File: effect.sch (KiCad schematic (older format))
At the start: 29 parts, among them U5 TL072

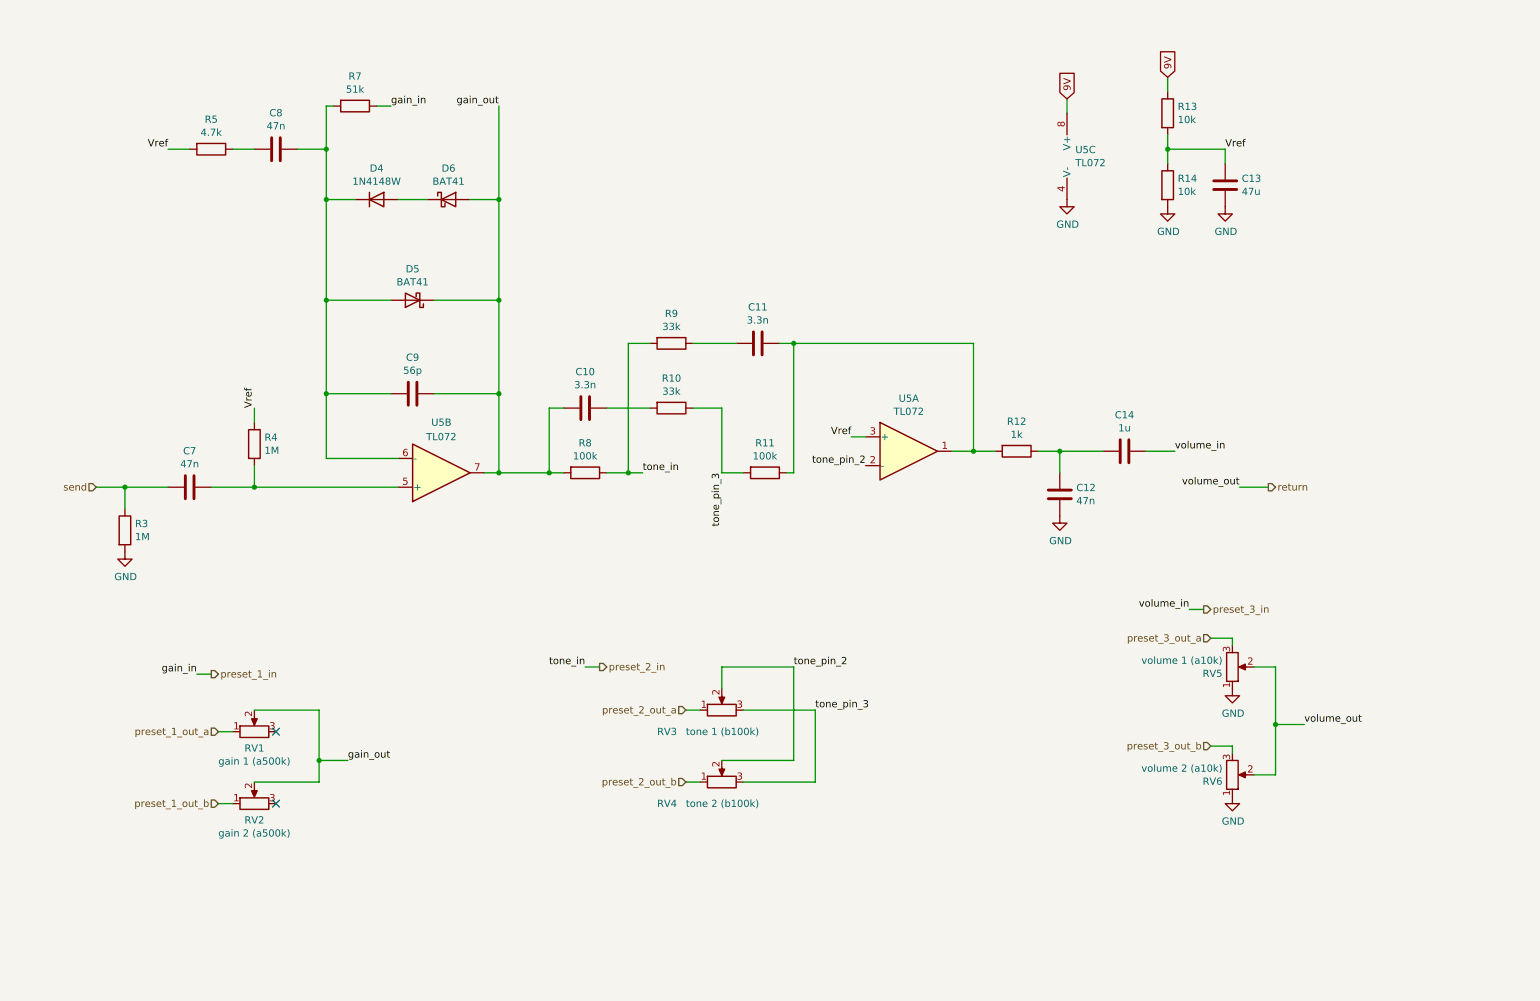
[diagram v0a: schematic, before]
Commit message: Use solid state switching and charge pump
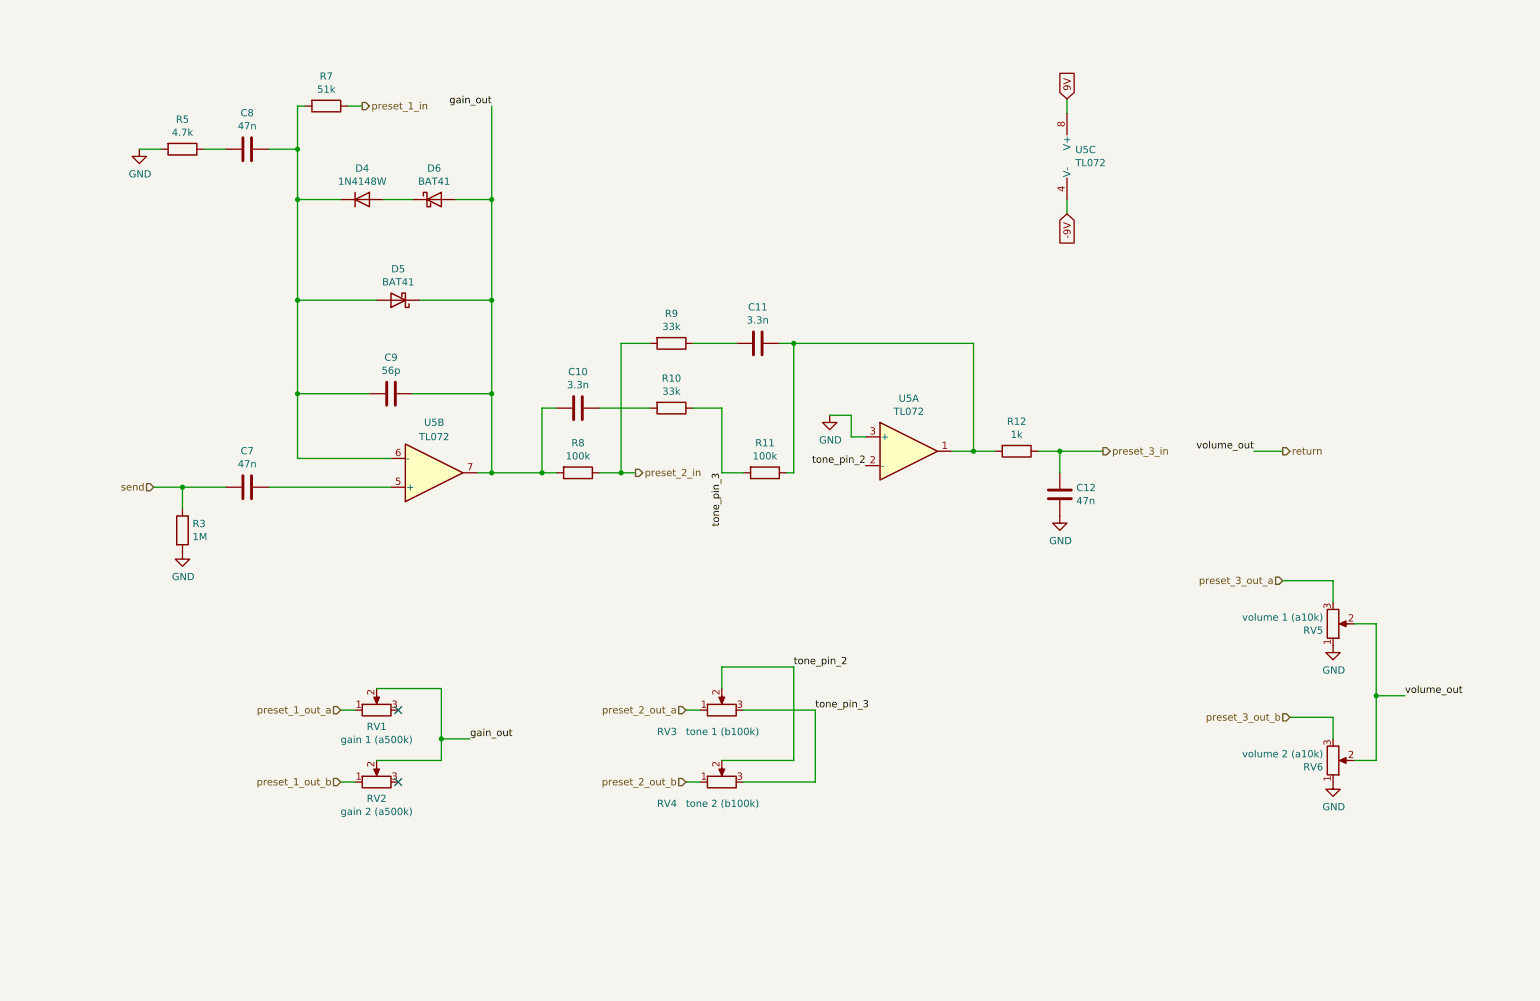
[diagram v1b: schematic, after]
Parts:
- removed C13: 47u, Capacitor_SMD:C_1206_3216Metric, symbol Device:C
- removed C14: 1u, Capacitor_SMD:C_0603_1608Metric, symbol Device:C
- removed R13, R14: 10k, Resistor_SMD:R_0603_1608Metric, symbol Device:R
- removed R4: 1M, Resistor_SMD:R_0603_1608Metric, symbol Device:R
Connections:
- net Vref is gone; now on net GND: R5.2, U5.3 (+)
- net GND: no longer U5.4 (V-)
- net preset_3_in: now also C12.2, R12.1
- new net -9V: U5.4 (V-)
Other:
- moved on the sheet: C10, C7, C8, C9, D4, D5, D6, R3, R5, R7, R8, RV1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

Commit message: Use 4053 switch, correct poor decisions made earlier
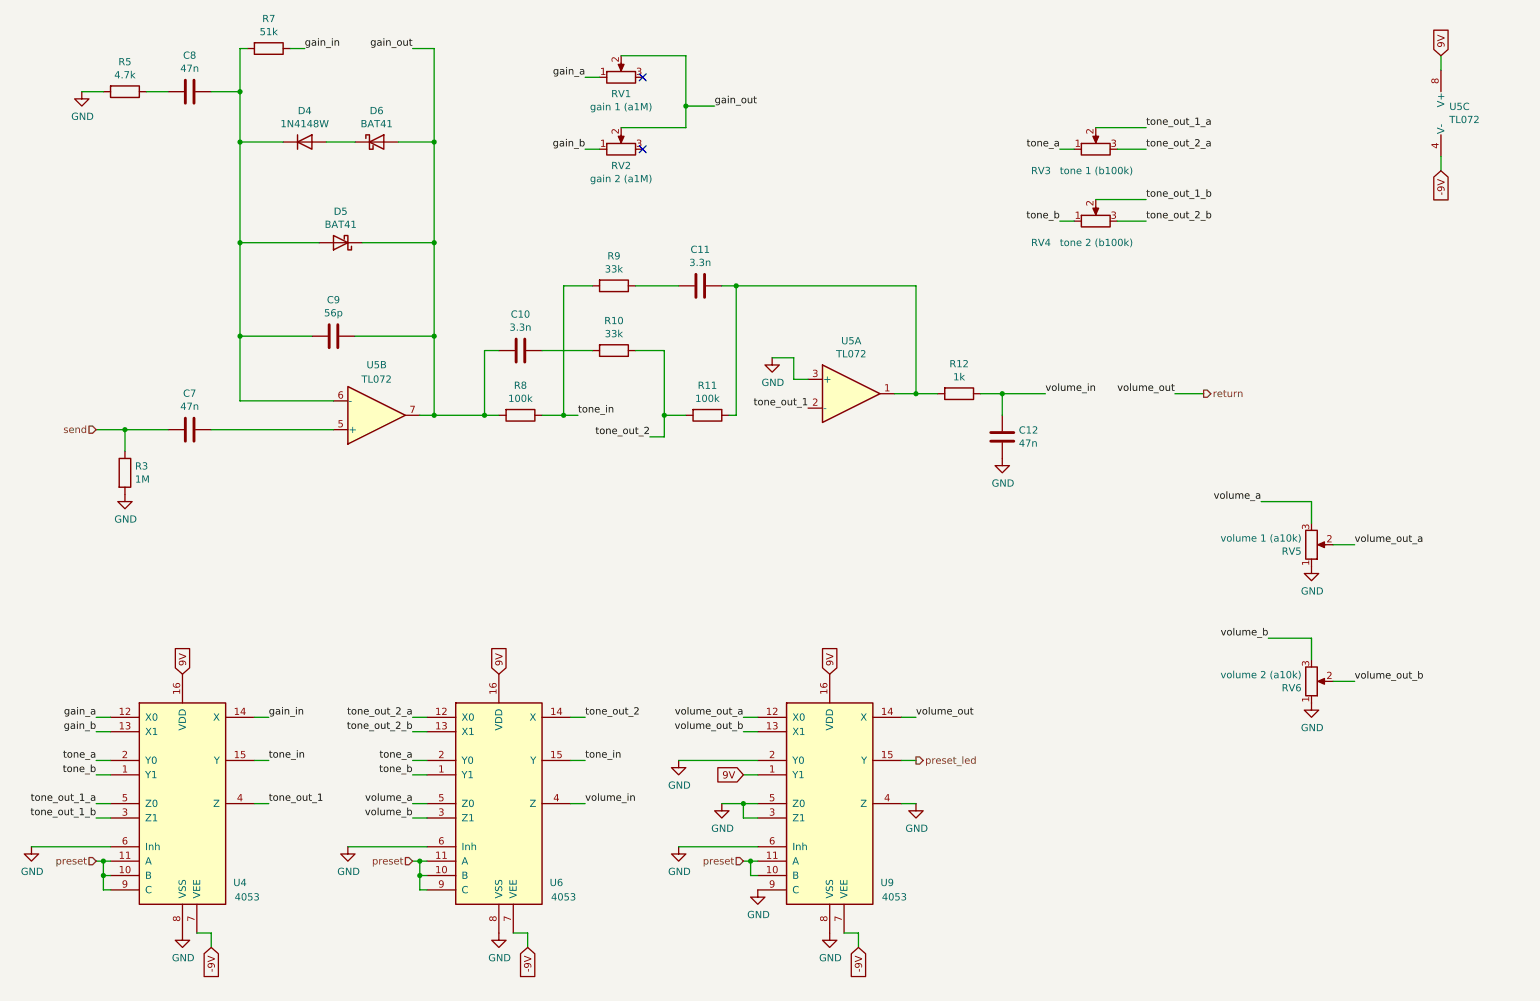
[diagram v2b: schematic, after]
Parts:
- added U4, U6, U9: 4053, symbol 4xxx:4053
- RV1: value gain 1 (a500k) -> gain 1 (a1M)
- RV2: value gain 2 (a500k) -> gain 2 (a1M)
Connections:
- net -9V: now also U4.7 (VEE), U6.7 (VEE), U9.7 (VEE)
- net 9V: now also U4.16 (VDD), U6.16 (VDD), U9.1 (Y1), U9.16 (VDD)
- net GND: now also U4.6 (Inh), U4.8 (VSS), U6.6 (Inh), U6.8 (VSS), U9.2 (Y0), U9.3 (Z1), U9.4 (Z), U9.5 (Z0), U9.6 (Inh), U9.8 (VSS), U9.9 (C)
- net return: now also U9.14 (X); no longer RV5.2, RV6.2
- net preset_1_in renamed gain_in
- net gain_in: now also U4.14 (X)
- net preset_1_out_a renamed gain_a
- net gain_a: now also U4.12 (X0)
- net preset_1_out_b renamed gain_b
- net gain_b: now also U4.13 (X1)
- net preset_2_in renamed tone_in
- net tone_in: now also U4.15 (Y), U6.15 (Y)
- net preset_2_out_a renamed tone_a
- net tone_a: now also U4.2 (Y0), U6.2 (Y0)
- net preset_2_out_b renamed tone_b
- net tone_b: now also U4.1 (Y1), U6.1 (Y1)
- net preset_3_in renamed volume_in
- net volume_in: now also U6.4 (Z)
- net preset_3_out_a renamed volume_a
- net volume_a: now also U6.5 (Z0)
- net preset_3_out_b renamed volume_b
- net volume_b: now also U6.3 (Z1)
- removed net tone_pin_2: RV3.2, RV4.2, U5.2 (-)
- net tone_pin_3 renamed tone_out_2
- net tone_out_2: now also U6.14 (X); no longer RV3.3, RV4.3
- new net preset: U4.10 (B), U4.11 (A), U4.9 (C), U6.10 (B), U6.11 (A), U6.9 (C), U9.10 (B), U9.11 (A)
- new net preset_led: U9.15 (Y)
- new net tone_out_1: U4.4 (Z), U5.2 (-)
- new net tone_out_1_a: RV3.2, U4.5 (Z0)
- new net tone_out_1_b: RV4.2, U4.3 (Z1)
- new net tone_out_2_a: RV3.3, U6.12 (X0)
- new net tone_out_2_b: RV4.3, U6.13 (X1)
- new net volume_out_a: RV5.2, U9.12 (X0)
- new net volume_out_b: RV6.2, U9.13 (X1)
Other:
- moved on the sheet: C10, C11, C12, C7, C8, C9, D4, D5, D6, R10, R11, R12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

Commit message: Fix a few issues
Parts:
- removed U9: 4053, symbol 4xxx:4053
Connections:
- net return: now also U6.4 (Z)
- net tone_a: no longer U6.2 (Y0)
- net tone_b: no longer U6.1 (Y1)
- net tone_in: no longer U6.15 (Y)
- net volume_a: now also U6.2 (Y0); no longer U6.5 (Z0)
- net volume_b: now also U6.1 (Y1); no longer U6.3 (Z1)
- net volume_in: now also U6.15 (Y); no longer U6.4 (Z)
- net volume_out_a: now also U6.5 (Z0)
- net volume_out_b: now also U6.3 (Z1)
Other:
- moved on the sheet: C10, C11, C12, C7, C8, C9, D4, D5, D6, R10, R11, R12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

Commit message: Reformatting
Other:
- moved on the sheet: RV5, RV6
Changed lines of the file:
@@
 	5550 4950 5500 4950
 Wire Wire Line
-	5950 4700 6050 4700
+	5950 4900 6050 4900
 Wire Wire Line
 	6800 4050 6800 4800
@@
 	0    -1   -1   0
 $EndComp
-Text Label 6050 4900 2    50   ~ 0
+Text Label 6050 4700 2    50   ~ 0
 tone_out_1
 $Comp
@@
 L Device:R_POT RV5
 U 1 1 60BBD12D
-P 10150 5150
-F 0 "RV5" H 10081 5196 50  0000 R CNN
-F 1 "volume 1 (a10k)" H 10081 5105 50  0000 R CNN
-F 2 "Potentiometer_THT:alpha_pot_16mm" H 10150 5150 50  0001 C CNN
-F 3 "~" H 10150 5150 50  0001 C CNN
-	1    10150 5150
+P 8850 4500
+F 0 "RV5" H 8781 4546 50  0000 R CNN
+F 1 "volume 1 (a10k)" H 8781 4455 50  0000 R CNN
+F 2 "Potentiometer_THT:alpha_pot_16mm" H 8850 4500 50  0001 C CNN
+F 3 "~" H 8850 4500 50  0001 C CNN
+	1    8850 4500
 	1    0    0    1
 $EndComp
@@
 L power:GND #PWR024
 U 1 1 60BBD127
-P 10150 5300
-F 0 "#PWR024" H 10150 5050 50  0001 C CNN
-F 1 "GND" H 10155 5127 50  0000 C CNN
-F 2 "" H 10150 5300 50  0001 C CNN
-F 3 "" H 10150 5300 50  0001 C CNN
-	1    10150 5300
+P 8850 4650
+F 0 "#PWR024" H 8850 4400 50  0001 C CNN
+F 1 "GND" H 8855 4477 50  0000 C CNN
+F 2 "" H 8850 4650 50  0001 C CNN
+F 3 "" H 8850 4650 50  0001 C CNN
+	1    8850 4650
 	1    0    0    -1
 $EndComp
@@
 L Device:R_POT RV6
 U 1 1 60C27070
-P 10150 6000
-F 0 "RV6" H 10081 6046 50  0000 R CNN
-F 1 "volume 2 (a10k)" H 10081 5955 50  0000 R CNN
-F 2 "Potentiometer_THT:alpha_pot_16mm" H 10150 6000 50  0001 C CNN
-F 3 "~" H 10150 6000 50  0001 C CNN
-	1    10150 6000
+P 8850 5350
+F 0 "RV6" H 8781 5396 50  0000 R CNN
+F 1 "volume 2 (a10k)" H 8781 5305 50  0000 R CNN
+F 2 "Potentiometer_THT:alpha_pot_16mm" H 8850 5350 50  0001 C CNN
+F 3 "~" H 8850 5350 50  0001 C CNN
+	1    8850 5350
 	1    0    0    1
 $EndComp
@@
 L power:GND #PWR025
 U 1 1 60C27076
-P 10150 6150
-F 0 "#PWR025" H 10150 5900 50  0001 C CNN
-F 1 "GND" H 10155 5977 50  0000 C CNN
-F 2 "" H 10150 6150 50  0001 C CNN
-F 3 "" H 10150 6150 50  0001 C CNN
-	1    10150 6150
-	1    0    0    -1
-$EndComp
-Wire Wire Line
-	10300 6000 10450 6000
-Wire Wire Line
-	10450 5150 10300 5150
-Wire Wire Line
-	10150 4850 10150 5000
+P 8850 5500
+F 0 "#PWR025" H 8850 5250 50  0001 C CNN
+F 1 "GND" H 8855 5327 50  0000 C CNN
+F 2 "" H 8850 5500 50  0001 C CNN
+F 3 "" H 8850 5500 50  0001 C CNN
+	1    8850 5500
+	1    0    0    -1
+$EndComp
+Wire Wire Line
+	9000 5350 9150 5350
+Wire Wire Line
+	9150 4500 9000 4500
+Wire Wire Line
+	8850 4200 8850 4350
 $Comp
 L Amplifier_Operational:TL072 U5
 U 1 1 60C594E9
 P 6350 4800
-F 0 "U5" H 6350 5167 50  0000 C CNN
-F 1 "TL072" H 6350 5076 50  0000 C CNN
+F 0 "U5" H 6400 4450 50  0000 C CNN
+F 1 "TL072" H 6400 4550 50  0000 C CNN
 F 2 "Package_SO:SOIC-8_3.9x4.9mm_P1.27mm" H 6350 4800 50  0001 C CNN
 F 3 "http://www.ti.com/lit/ds/symlink/tl071.pdf" H 6350 4800 50  0001 C CNN
 F 4 "C6961" H 6350 4800 50  0001 C CNN "LCSC"
 	1    6350 4800
-	1    0    0    -1
+	1    0    0    1
 $EndComp
 $Comp
@@
 	7700 4800 7400 4800
 Connection ~ 7400 4800
-Text Label 8600 4800 2    50   ~ 0
+Text Label 10100 4800 2    50   ~ 0
 volume_out
 Wire Wire Line
-	8800 4800 8600 4800
-Text HLabel 8800 4800 2    50   Output ~ 0
+	10300 4800 10100 4800
+Text HLabel 10300 4800 2    50   Output ~ 0
 return
 Wire Wire Line
 	10450 1000 10450 1100
 Wire Wire Line
-	9850 5700 10150 5700
-Wire Wire Line
-	10150 5700 10150 5850
+	8550 5050 8850 5050
+Wire Wire Line
+	8850 5050 8850 5200
 Text GLabel 10450 1800 3    50   Input ~ 0
 -9V
 Wire Wire Line
 	10450 1800 10450 1700
-$Comp
-L power:GND #PWR021
-U 1 1 610A9824
-P 5800 4550
-F 0 "#PWR021" H 5800 4300 50  0001 C CNN
-F 1 "GND" H 5805 4377 50  0000 C CNN
-F 2 "" H 5800 4550 50  0001 C CNN
-F 3 "" H 5800 4550 50  0001 C CNN
-	1    5800 4550
-	1    0    0    -1
-$EndComp
-Wire Wire Line
-	5800 4550 5950 4550
-Wire Wire Line
-	5950 4550 5950 4700
 Wire Wire Line
 	1900 5050 2750 5050
 Wire Wire Line
-	9800 4850 10150 4850
+	8500 4200 8850 4200
 $Comp
 L power:GND #PWR0101
@@
 Wire Wire Line
 	6300 1750 6200 1750
-Text GLabel 5900 3050 3    50   Input ~ 0
+Text GLabel 5900 2950 2    50   Input ~ 0
 -9V
 $Comp
@@
 Wire Wire Line
 	5800 2950 5900 2950
-Wire Wire Line
-	5900 2950 5900 3050
 Text GLabel 5700 1150 1    50   Input ~ 0
 9V
@@
 L power:GND #PWR?
 U 1 1 610BAB65
-P 4650 2350
+P 5050 2250
 AR Path="/610BAB65" Ref="#PWR?"  Part="1"
 AR Path="/60B9FFB7/610BAB65" Ref="#PWR027"  Part="1"
-F 0 "#PWR027" H 4650 2100 50  0001 C CNN
-F 1 "GND" H 4655 2177 50  0000 C CNN
-F 2 "" H 4650 2350 50  0001 C CNN
-F 3 "" H 4650 2350 50  0001 C CNN
-	1    4650 2350
+F 0 "#PWR027" H 5050 2000 50  0001 C CNN
+F 1 "GND" H 4900 2200 50  0000 C CNN
+F 2 "" H 5050 2250 50  0001 C CNN
+F 3 "" H 5050 2250 50  0001 C CNN
+	1    5050 2250
 	1    0    0    -1
 $EndComp
@@
 Wire Wire Line
 	5100 1450 5200 1450
-Wire Wire Line
-	4650 2350 5200 2350
 Text Label 2550 2400 0    50   ~ 0
 gain_in
@@
 Text Label 7700 4800 0    50   ~ 0
 volume_in
-Text Label 9800 4850 2    50   ~ 0
+Text Label 8500 4200 2    50   ~ 0
 volume_a
-Text Label 9850 5700 2    50   ~ 0
+Text Label 8550 5050 2    50   ~ 0
 volume_b
 Text HLabel 5100 2450 0    50   Input ~ 0
@@
 Wire Wire Line
 	8650 1450 8550 1450
-Text GLabel 8250 3050 3    50   Input ~ 0
+Text GLabel 8250 2950 2    50   Input ~ 0
 -9V
 $Comp
@@
 Wire Wire Line
 	8150 2950 8250 2950
-Wire Wire Line
-	8250 2950 8250 3050
 Text GLabel 8050 1150 1    50   Input ~ 0
 9V
@@
 L power:GND #PWR?
 U 1 1 611A889A
-P 7000 2350
+P 7400 2250
 AR Path="/611A889A" Ref="#PWR?"  Part="1"
 AR Path="/60B9FFB7/611A889A" Ref="#PWR029"  Part="1"
-F 0 "#PWR029" H 7000 2100 50  0001 C CNN
-F 1 "GND" H 7005 2177 50  0000 C CNN
-F 2 "" H 7000 2350 50  0001 C CNN
-F 3 "" H 7000 2350 50  0001 C CNN
-	1    7000 2350
+F 0 "#PWR029" H 7400 2000 50  0001 C CNN
+F 1 "GND" H 7250 2200 50  0000 C CNN
+F 2 "" H 7400 2250 50  0001 C CNN
+F 3 "" H 7400 2250 50  0001 C CNN
+	1    7400 2250
 	1    0    0    -1
 $EndComp
@@
 Wire Wire Line
 	7450 1450 7550 1450
-Wire Wire Line
-	7000 2350 7550 2350
 Wire Wire Line
 	7500 2450 7500 2550
@@
 Text Label 8650 2050 0    50   ~ 0
 volume_out
-Text Label 10450 5150 0    50   ~ 0
+Text Label 9150 4500 0    50   ~ 0
 volume_out_a
-Text Label 10450 6000 0    50   ~ 0
+Text Label 9150 5350 0    50   ~ 0
 volume_out_b
+$Comp
+L power:GND #PWR?
+U 1 1 614849D6
+P 5950 4900
+F 0 "#PWR?" H 5950 4650 50  0001 C CNN
+F 1 "GND" H 5955 4727 50  0000 C CNN
+F 2 "" H 5950 4900 50  0001 C CNN
+F 3 "" H 5950 4900 50  0001 C CNN
+	1    5950 4900
+	1    0    0    -1
+$EndComp
+Wire Wire Line
+	5050 2250 5200 2250
+Wire Wire Line
+	5200 2250 5200 2350
+Wire Wire Line
+	7400 2250 7550 2250
+Wire Wire Line
+	7550 2250 7550 2350
 $EndSCHEMATC
